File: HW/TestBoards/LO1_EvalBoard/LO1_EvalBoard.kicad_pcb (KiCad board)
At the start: 2 copper layers, 50 x 40 mm, 21 parts, among them J1 SMA, J2 Conn_01x05, U2 CY2-44+, U3 HMC516, Y1 HMC506LP4

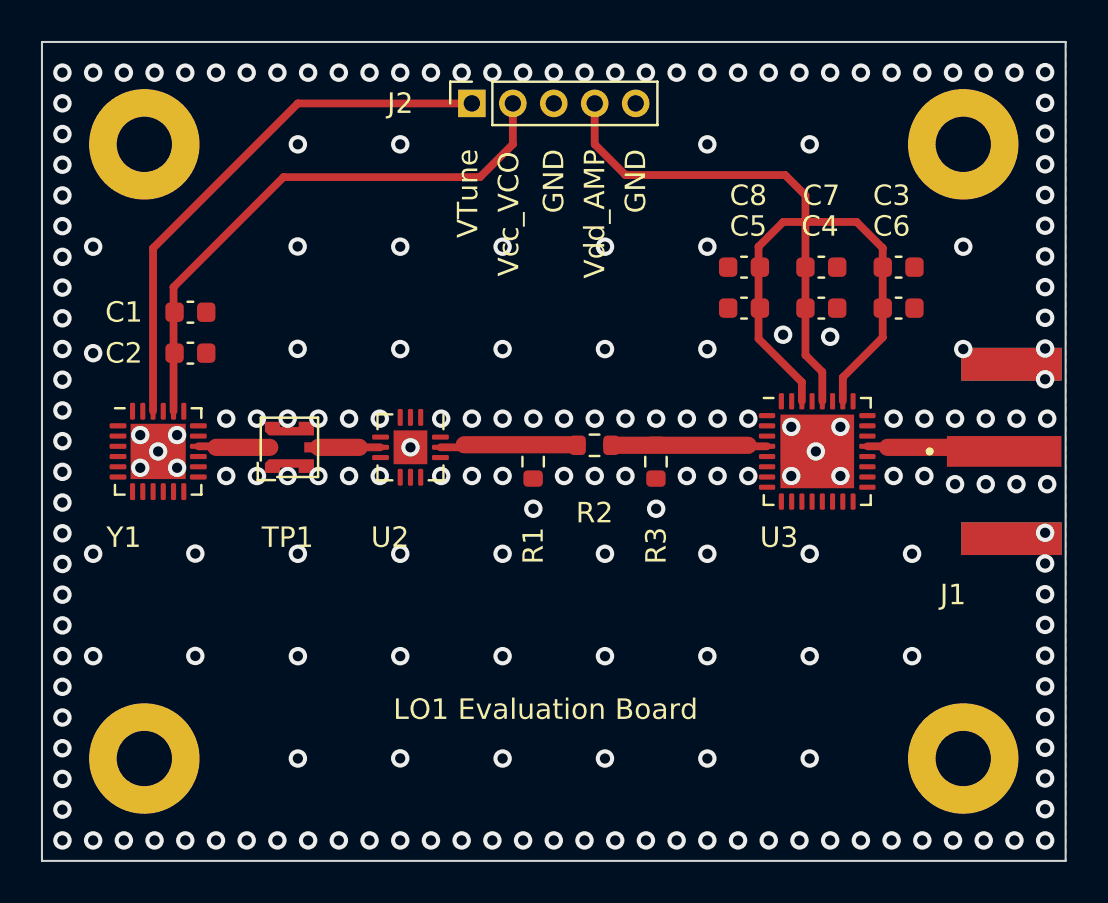
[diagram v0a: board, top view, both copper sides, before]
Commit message: All Test Boards developed
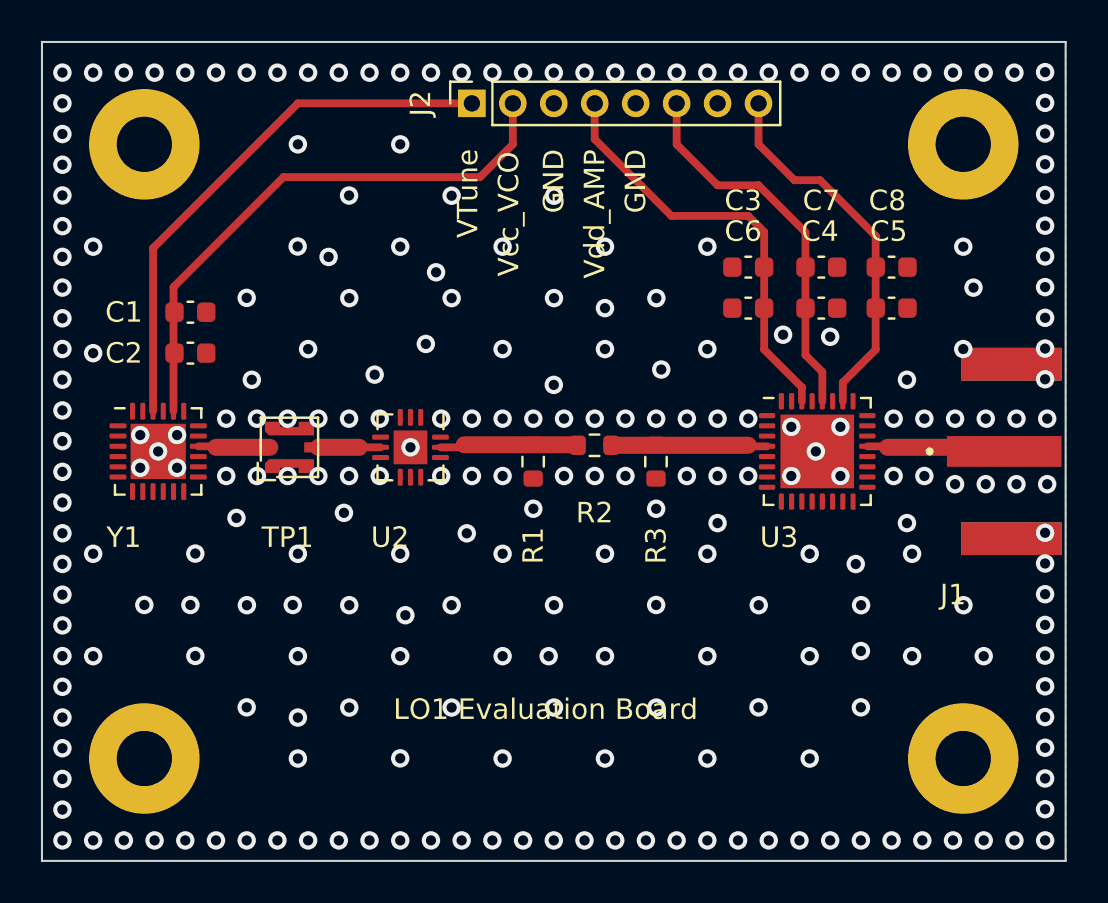
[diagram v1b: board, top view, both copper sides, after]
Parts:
- J2: value Conn_01x05 -> Conn_01x08; footprint Connector_PinSocket_2.00mm:PinSocket_1x05_P2.00mm_Vertical -> Connector_PinSocket_2.00mm:PinSocket_1x08_P2.00mm_Vertical
- moved C3 7.34 mm to (169.5, 83.0), turned to 180 degrees
- moved C6 7.34 mm to (169.5, 81.0), turned to 180 degrees
- moved C5 7.21 mm to (176.5, 81.0), turned to 0 degrees
- moved C8 7.21 mm to (176.5, 83.0), turned to 0 degrees
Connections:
- C3 pad 1: /Vdd_Amp -> /Vdd_Amp1
- C4 pad 1: /Vdd_Amp -> /Vdd_Amp2
- C5 pad 1: /Vdd_Amp -> /Vdd_Amp3
- C6 pad 1: /Vdd_Amp -> /Vdd_Amp1
- C7 pad 1: /Vdd_Amp -> /Vdd_Amp2
- C8 pad 1: /Vdd_Amp -> /Vdd_Amp3
- J2 pad 4: /Vdd_Amp -> /Vdd_Amp1
- U3 pad 26: /Vdd_Amp -> /Vdd_Amp3
- U3 pad 28: /Vdd_Amp -> /Vdd_Amp2
- U3 pad 30: /Vdd_Amp -> /Vdd_Amp1
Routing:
- net /Vdd_Amp: track 47.5 -> 0.00 mm
- net /Vdd_Amp1: track 0.00 -> 20.9 mm
- net /Vdd_Amp2: track 0.00 -> 18.7 mm
- net /Vdd_Amp3: track 0.00 -> 18.3 mm
- net GND: vias 211 -> 255
